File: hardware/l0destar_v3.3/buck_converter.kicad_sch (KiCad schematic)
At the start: 14 parts

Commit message: schematic<>readme discrepency fixes
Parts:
- S6C1: value 0402 100nF 25V 10% X7R -> 0402 100nF 50V 10% X7R; Manufacturer_Name Multicomp Pro -> Murata; Manufacturer_Part_Number MC0402B104K250CT -> GRM155R71H104KE14D
- S6C2: value 0402 1uF 10V 10% X7R -> 0603 2.2uF 25V 10% X7R; footprint Capacitor_SMD:C_0402_1005Metric -> Resistor_SMD:R_0603_1608Metric
- S6C4: value 0402 10pF 10V C0G/NP0 -> 0402 10pF 50V C0G/NP0
- S6C8: Manufacturer_Name Taiyo Yuden -> Murata; Manufacturer_Part_Number MCASU105SB7104KFNA01 -> GRM155R71H104KE14D
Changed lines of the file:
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@@
 			)
 		)
-		(property "Value" "0402 100nF 25V 10% X7R"
+		(property "Value" "0402 100nF 50V 10% X7R"
 			(at 28.956 43.434 0)
 			(show_name no)
@@
 			)
 		)
-		(property "Datasheet" "https://uk.farnell.com/multicomp-pro/mc0402b104k250ct/cap-0-1-f-25v-10-x7r-0402/dp/2320759"
+		(property "Datasheet" ""
 			(at 25.4 41.91 0)
 			(hide yes)
@@
 			)
 		)
-		(property "Description" "Unpolarized capacitor"
+		(property "Description" ""
 			(at 25.4 41.91 0)
 			(hide yes)
@@
 			)
 		)
-		(property "Manufacturer_Part_Number" "MC0402B104K250CT"
+		(property "Manufacturer_Part_Number" "GRM155R71H104KE14D"
 			(at 25.4 41.91 0)
 			(hide yes)
@@
 			)
 		)
-		(property "Manufacturer_Name" "Multicomp Pro"
+		(property "Manufacturer_Name" "Murata"
 			(at 25.4 41.91 0)
 			(hide yes)
@@
 			)
 		)
-		(property "Datasheet" "https://ds.yuden.co.jp/TYCOMPAS/or/detail?pn=MCASU105SB7104KFNA01&u=M"
+		(property "Datasheet" ""
 			(at 167.64 60.96 0)
 			(hide yes)
@@
 			)
 		)
-		(property "Description" "Unpolarized capacitor"
+		(property "Description" ""
 			(at 167.64 60.96 0)
 			(hide yes)
@@
 			)
 		)
-		(property "Manufacturer_Part_Number" "MCASU105SB7104KFNA01"
+		(property "Manufacturer_Part_Number" "GRM155R71H104KE14D"
 			(at 167.64 60.96 0)
 			(hide yes)
@@
 			)
 		)
-		(property "Manufacturer_Name" "Taiyo Yuden"
+		(property "Manufacturer_Name" "Murata"
 			(at 167.64 60.96 0)
 			(hide yes)
@@
 			)
 		)
-		(property "Value" "0402 1uF 10V 10% X7R"
+		(property "Value" "0603 2.2uF 25V 10% X7R"
 			(at 23.495 64.135 0)
 			(show_name no)
@@
 			)
 		)
-		(property "Footprint" "Capacitor_SMD:C_0402_1005Metric"
+		(property "Footprint" "Resistor_SMD:R_0603_1608Metric"
 			(at 39.0652 73.66 0)
 			(hide yes)
@@
 			)
 		)
-		(property "Value" "0402 10pF 10V C0G/NP0"
+		(property "Value" "0402 10pF 50V C0G/NP0"
 			(at 140.97 83.185 90)
 			(show_name no)

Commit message: revised 3.3 board, parts and readme updates
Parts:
- S6C2: footprint Resistor_SMD:R_0603_1608Metric -> Capacitor_SMD:C_0603_1608Metric
- S6R2: value 0402 226K 1% -> 0402 226K 1% ANTI-SULFUR AEC-Q200
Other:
- note added: "31/08/2026"
- note added: "ANTI-SULFUR RESISTORS (AEC-Q200 recommended) S6R2 - FB divider, bottom. If this fails open the output voltage collapses. Safe failure mode but the BOM part is already anti-sulfur so advise keeping it to match the bottom half of the divider. S6R3 - FB divider, top. If this fails open the LT8609 sees no feedback and drives output to maximum leading to over-voltage downstream. Mitigated by OVP in sh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"
- note added: "Buck converter 12V -> 4.2V LT8609 reference implementation VOUT == 0.782V x (1 + S6R3/S6R2) == 4.24V 3-resistor divider added 28/08 to switch off if the supply falls below 3.3V uses hysteresis to avoid powering back on until the supply is over 4.6V revised spec of resistors to include anti-sulfur parts"
- note removed: "28/08/2026"
- note removed: "Buck converter 12V -> 4.2V LT8609 reference implementation VOUT == 0.782V x (1 + S6R3/S6R2) == 4.24V 3-resistor divider added 28/08 to switch off if the supply falls below 3.3V uses hysteresis to avoid powering back on until the supply is over 4.6V"
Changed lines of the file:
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@@
 	(generator_version "10.0")
 	(paper "A4")
-	(text "28/08/2026"
+	(text "31/08/2026"
 		(exclude_from_sim no)
 		(at 205.994 193.294 0)
@@
 		)
 	)
-	(text "Buck converter 12V -> 4.2V\nLT8609 reference implementation\nVOUT == 0.782V x (1 + S6R3/S6R2) == 4.24V\n3-resistor divider added 28/08 to switch off if the supply falls below 3.3V\nuses hysteresis to avoid powering back on until the supply is over 4.6V"
+	(text "Buck converter 12V -> 4.2V\nLT8609 reference implementation\nVOUT == 0.782V x (1 + S6R3/S6R2) == 4.24V\n3-resistor divider added 28/08 to switch off if the supply falls below 3.3V\nuses hysteresis to avoid powering back on until the supply is over 4.6V\nrevised spec of resistors to include anti-sulfur parts"
 		(exclude_from_sim no)
 		(at 179.705 173.355 0)
@@
 				(size 1.27 1.27)
 			)
+		)
+	)
+	(text "ANTI-SULFUR RESISTORS (AEC-Q200 recommended)\n\nS6R2 - FB divider, bottom. If this fails open the output voltage collapses. Safe failure mode but the BOM part is already anti-sulfur so advise keeping it to match the bottom half of the divider.\nS6R3 - FB divider, top. If this fails open the LT8609 sees no feedback and drives output to maximum leading to over-voltage downstream. Mitigated by OVP in sheet 11 but wise to use anti-sulfur here for defence in depth.\nS6R4 - Enable divider, top. If this fails open the board doesn't enable. Safe failure mode but bricks until resolved so fitting anti-sulfur here is sensible.\nS6R5 - Enable divider, bottom. If this fails the device may turn on in brown-out input voltage territory causing unexpected behaviour. Safe failure mode but still wise to use anti-sulfur.\n\nS6R3 is the only critical one for anti-sulfur, the others are recommended but fail safe.\n\nConformal coating is also recommended after build."
+		(exclude_from_sim no)
+		(at 18.415 146.05 0)
+		(effects
+			(font
+				(size 1.27 1.27)
+			)
+			(justify left)
 		)
 	)
@@
 		(dnp no)
 		(property "Reference" "S6R2"
-			(at 104.775 78.74 0)
-			(show_name no)
-			(do_not_autoplace no)
-			(effects
-				(font
-					(size 1.27 1.27)
-				)
-			)
-		)
-		(property "Value" "0402 226K 1%"
-			(at 104.775 81.28 0)
+			(at 92.71 83.185 0)
+			(show_name no)
+			(do_not_autoplace no)
+			(effects
+				(font
+					(size 1.27 1.27)
+				)
+			)
+		)
+		(property "Value" "0402 226K 1% ANTI-SULFUR AEC-Q200"
+			(at 92.71 85.725 0)
 			(show_name no)
 			(do_not_autoplace no)
@@
 			)
 		)
-		(property "Footprint" "Resistor_SMD:R_0603_1608Metric"
+		(property "Footprint" "Capacitor_SMD:C_0603_1608Metric"
 			(at 39.0652 73.66 0)
 			(hide yes)

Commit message: change resistor divider and a few parts
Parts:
- S6R5: value 0402 300K 1% ANTI-SULFUR AEC-Q200 -> 0402 243K 1% ANTI-SULFUR AEC-Q200
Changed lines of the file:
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@@
 			)
 		)
-		(property "Value" "0402 300K 1% ANTI-SULFUR AEC-Q200"
+		(property "Value" "0402 243K 1% ANTI-SULFUR AEC-Q200"
 			(at 107.95 120.015 0)
 			(show_name no)

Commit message: 300K is what we want
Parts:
- S6R5: value 0402 243K 1% ANTI-SULFUR AEC-Q200 -> 0402 300K 1% ANTI-SULFUR AEC-Q200
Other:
- note added: "Output voltage divider: 0.782V x (1 + S6R3/S6R2) == 4.24V Enable divider: EN threshold: 1.05V rising, 1.00V falling. VOUT = 4.24V K = 1 + S6R4/S6R5 + S6R4/S6R6 VIN_on = K x 1.05 -> 4.82V VIN_off = K x 1.00 - S6R4 x VOUT / S6R6 -> 3.51V Note: VIN_off very likely does not satisfy ISO 16750-2, this is deliberate. Bench tests using a Riden RD6006 power supply, a v3.1 board and firmware modified to de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"
- moved on the sheet: S6C1, S6C2, S6C3, S6C4, S6C5, S6C8, S6L1, S6R1, S6R2, S6R3, S6R4, S6R5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

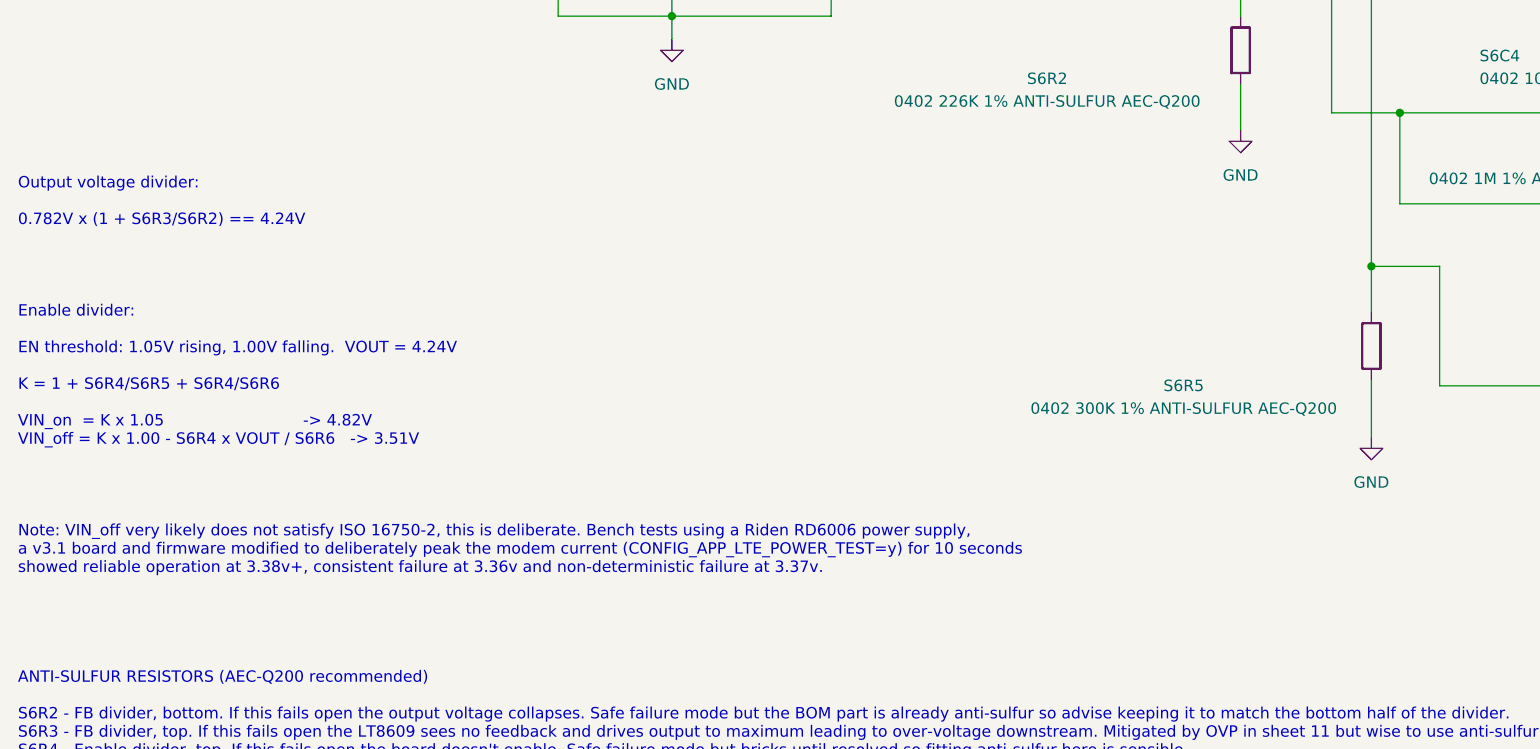
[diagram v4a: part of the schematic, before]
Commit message: 243K, changed my mind. hysteresis doesn't actually work if EN never goes low
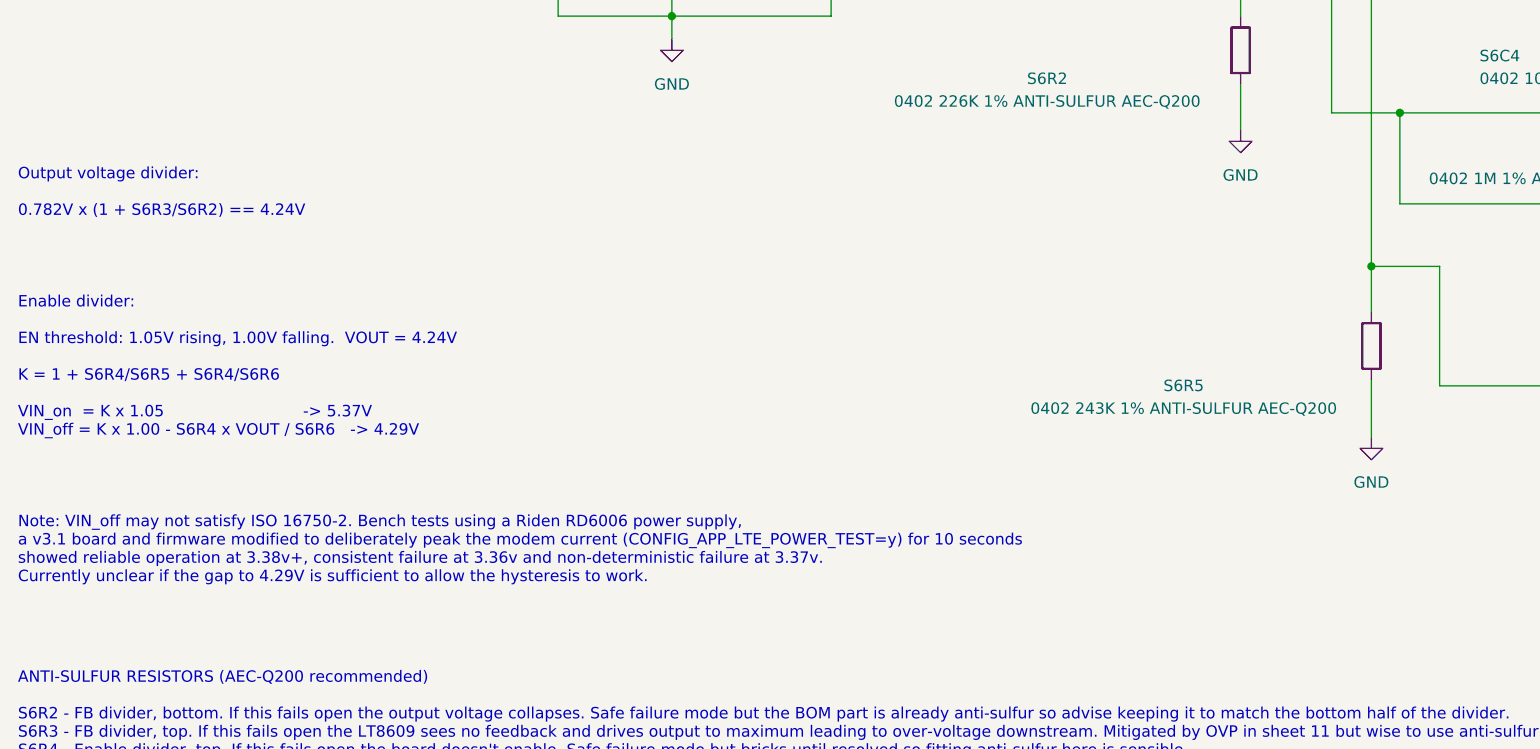
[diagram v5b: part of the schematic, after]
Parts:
- S6R5: value 0402 300K 1% ANTI-SULFUR AEC-Q200 -> 0402 243K 1% ANTI-SULFUR AEC-Q200; Manufacturer_Name Panasonic -> (none); Manufacturer_Part_Number ERJ2RKF1004X -> (none)
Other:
- note added: "Output voltage divider: 0.782V x (1 + S6R3/S6R2) == 4.24V Enable divider: EN threshold: 1.05V rising, 1.00V falling. VOUT = 4.24V K = 1 + S6R4/S6R5 + S6R4/S6R6 VIN_on = K x 1.05 -> 5.37V VIN_off = K x 1.00 - S6R4 x VOUT / S6R6 -> 4.29V Note: VIN_off may not satisfy ISO 16750-2. Bench tests using a Riden RD6006 power supply, a v3.1 board and firmware modified to deliberately peak the modem current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"
- note removed: "Output voltage divider: 0.782V x (1 + S6R3/S6R2) == 4.24V Enable divider: EN threshold: 1.05V rising, 1.00V falling. VOUT = 4.24V K = 1 + S6R4/S6R5 + S6R4/S6R6 VIN_on = K x 1.05 -> 4.82V VIN_off = K x 1.00 - S6R4 x VOUT / S6R6 -> 3.51V Note: VIN_off very likely does not satisfy ISO 16750-2, this is deliberate. Bench tests using a Riden RD6006 power supply, a v3.1 board and firmware modified to de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"
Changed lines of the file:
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@@
 		)
 	)
-	(text "Output voltage divider:\n\n0.782V x (1 + S6R3/S6R2) == 4.24V\n\n\n\n\nEnable divider:\n\nEN threshold: 1.05V rising, 1.00V falling.  VOUT = 4.24V\n\nK = 1 + S6R4/S6R5 + S6R4/S6R6\n\nVIN_on  = K x 1.05                            -> 4.82V\nVIN_off = K x 1.00 - S6R4 x VOUT / S6R6   -> 3.51V\n\n\n\n\nNote: VIN_off very likely does not satisfy ISO 16750-2, this is deliberate. Bench tests using a Riden RD6006 power supply,\na v3.1 board and firmware modified to deliberately peak the modem current (CONFIG_APP_LTE_POWER_TEST=y) for 10 seconds\nshowed reliable operation at 3.38v+, consistent failure at 3.36v and non-deterministic failure at 3.37v.\n\n"
+	(text "Output voltage divider:\n\n0.782V x (1 + S6R3/S6R2) == 4.24V\n\n\n\n\nEnable divider:\n\nEN threshold: 1.05V rising, 1.00V falling.  VOUT = 4.24V\n\nK = 1 + S6R4/S6R5 + S6R4/S6R6\n\nVIN_on  = K x 1.05                            -> 5.37V\nVIN_off = K x 1.00 - S6R4 x VOUT / S6R6   -> 4.29V\n\n\n\n\nNote: VIN_off may not satisfy ISO 16750-2. Bench tests using a Riden RD6006 power supply,\na v3.1 board and firmware modified to deliberately peak the modem current (CONFIG_APP_LTE_POWER_TEST=y) for 10 seconds\nshowed reliable operation at 3.38v+, consistent failure at 3.36v and non-deterministic failure at 3.37v.\nCurrently unclear if the gap to 4.29V is sufficient to allow the hysteresis to work.\n\n"
 		(exclude_from_sim no)
 		(at 18.415 116.84 0)
@@
 			)
 		)
-		(property "Value" "0402 300K 1% ANTI-SULFUR AEC-Q200"
+		(property "Value" "0402 243K 1% ANTI-SULFUR AEC-Q200"
 			(at 148.59 119.38 0)
 			(show_name no)
@@
 			)
 		)
-		(property "Datasheet" "https://industrial.panasonic.com/cdbs/www-data/pdf/RDA0000/AOA0000C304.pdf"
+		(property "Datasheet" ""
 			(at 169.545 112.395 0)
 			(hide yes)
@@
 			)
 		)
-		(property "Description" "Resistor"
+		(property "Description" ""
 			(at 169.545 112.395 0)
 			(hide yes)
@@
 			)
 		)
-		(property "Manufacturer_Part_Number" "ERJ2RKF1004X"
+		(property "Manufacturer_Part_Number" ""
 			(at 169.545 112.395 0)
 			(hide yes)
@@
 			)
 		)
-		(property "Manufacturer_Name" "Panasonic"
+		(property "Manufacturer_Name" ""
 			(at 169.545 112.395 0)
 			(hide yes)
